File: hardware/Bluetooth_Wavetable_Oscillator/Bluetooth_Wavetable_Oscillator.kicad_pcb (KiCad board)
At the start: 2 copper layers, 48 x 110 mm, 65 parts, among them J1 2x5 Connector, J2 AudioJack2, J3 AudioJack2_SwitchT, J4 AudioJack2_SwitchT, SW1 SW_Push, U1 L7805, U2 ESP32-WROOM-32D, U3 MCP4821, U4 TL074, U5 TL072, U6 NE5532

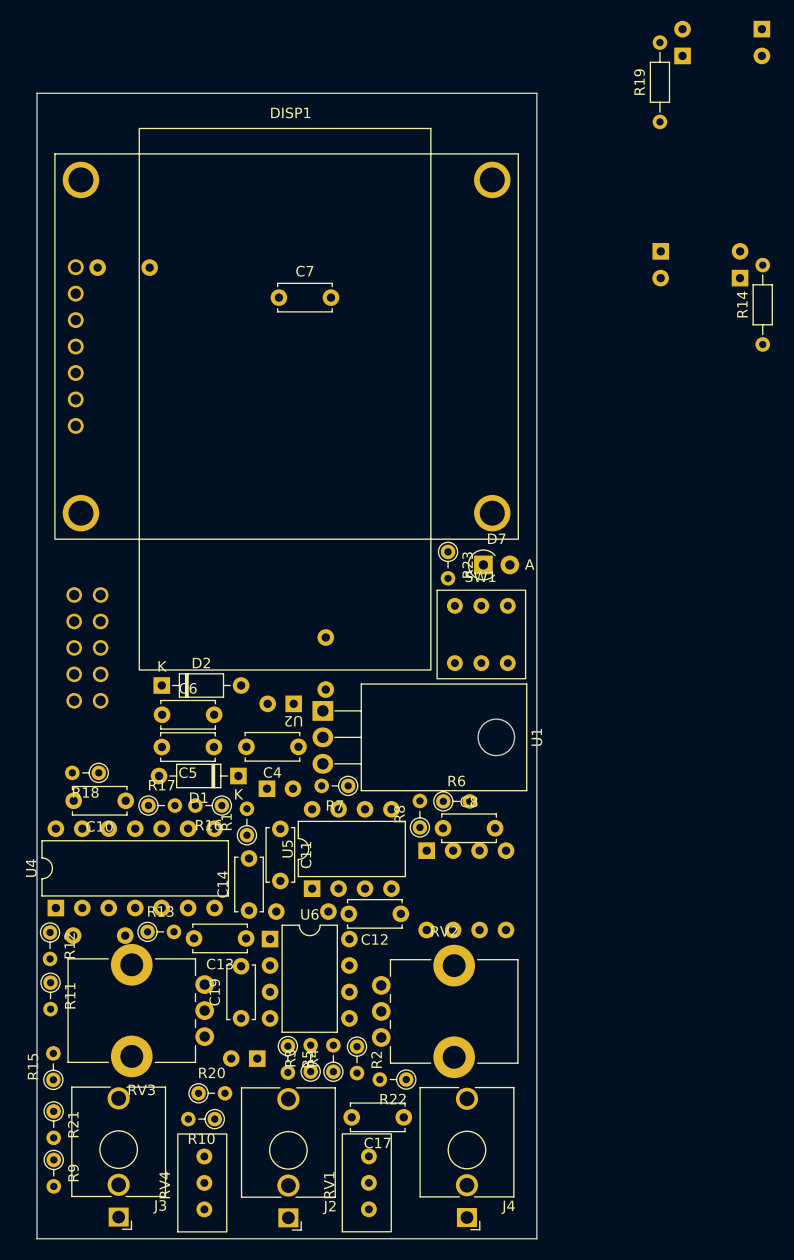
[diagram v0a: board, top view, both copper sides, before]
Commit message: update shematic, PCB and footprints
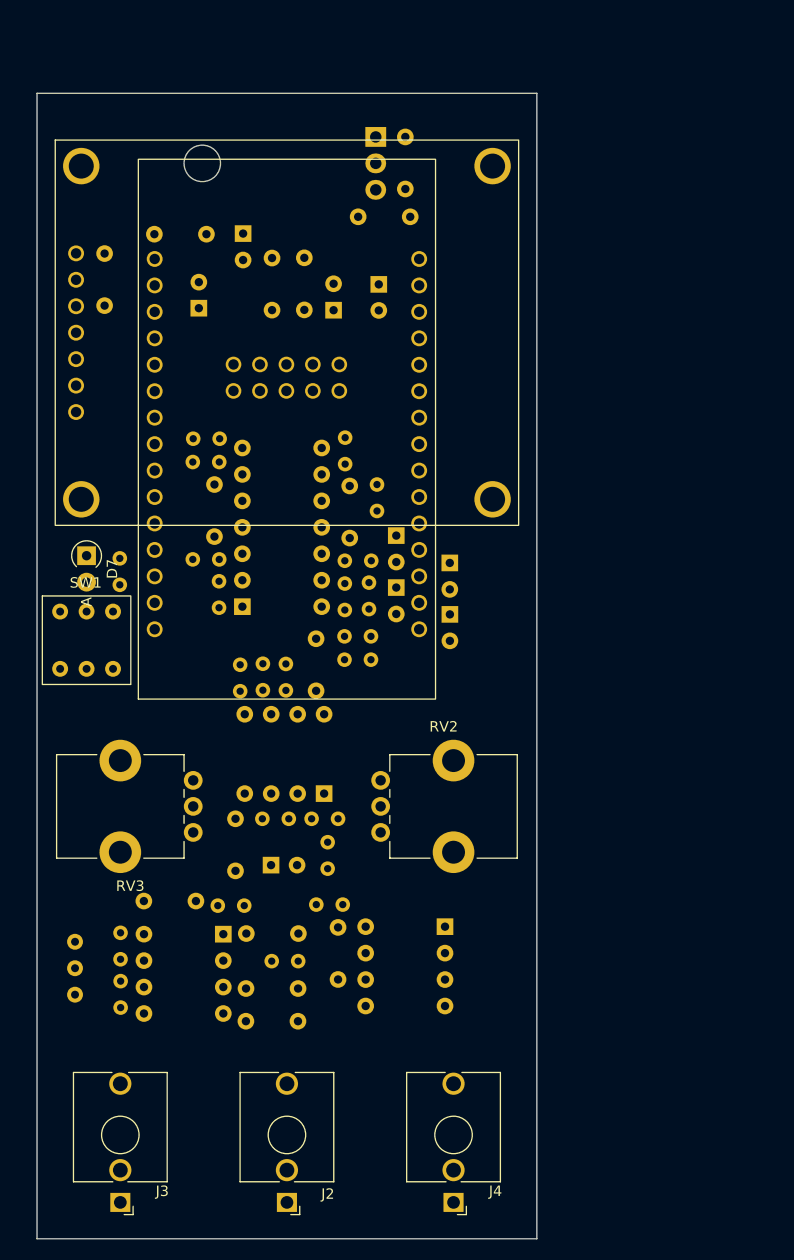
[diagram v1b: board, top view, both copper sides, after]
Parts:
- removed C17: 0.1u, Capacitor_THT:C_Disc_D5.0mm_W2.5mm_P5.00mm
- removed RV1: 10k, Trimmer-potentiometer:Trimmer-potentiometer
- C10, C11, C12, C13, C14, C19, C4, C5, C6, C7, C8, R1, R10, R11, R12, R13, R15, R16, R17, R18, R2, R20, R21, R22, R23, R3, R5, R6, R7, R8, R9, RV4, U1, U4, U5, U6: moved to B.Cu
- D1, D2: footprint Diode_THT:D_DO-35_SOD27_P7.62mm_Horizontal -> Diode_THT:D_DO-35_SOD27_P2.54mm_Vertical_KathodeUp; moved to B.Cu
- D3, D4, D5, D6: footprint Diode_THT:D_DO-35_SOD27_P7.62mm_Horizontal -> Diode_THT:D_DO-35_SOD27_P2.54mm_Vertical_KathodeUp
- R14, R19: footprint Resistor_THT:R_Axial_DIN0204_L3.6mm_D1.6mm_P7.62mm_Horizontal -> Resistor_THT:R_Axial_DIN0204_L3.6mm_D1.6mm_P2.54mm_Vertical; moved to B.Cu
- R4: value 10k -> 1k; moved to B.Cu
- moved R15 62.9 mm to (153.7, 85.4)
- moved D6 60.0 mm to (155.6, 87.8), turned to -90 degrees
- moved D5 58.0 mm to (155.6, 92.8), turned to -90 degrees
- moved R19 57.9 mm to (150.6, 97.4), turned to 0 degrees
- moved U1 55.4 mm to (153.6, 49.5)
- moved R10 53.8 mm to (136.0, 90.0), turned to 0 degrees
- moved C1 53.6 mm to (156.4, 49.5), turned to -90 degrees
- moved D1 52.1 mm to (140.8, 58.8), turned to -90 degrees
- moved C4 51.2 mm to (151.9, 57.1), turned to 0 degrees
- moved R9 50.8 mm to (140.6, 100.2)
- moved R14 50.3 mm to (150.6, 99.7), turned to 0 degrees
- moved R12 48.0 mm to (138.6, 80.7), turned to 180 degrees
- moved R13 47.9 mm to (138.6, 78.5), turned to 180 degrees
- moved C5 47.3 mm to (143.6, 61.1), turned to -90 degrees
- moved C2 46.6 mm to (136.6, 65.9), turned to 90 degrees
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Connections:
- R4 pad 1: /Output/-1.024V -> Net-(R4-Pad1)
- R4 pad 2: Net-(U6B--) -> Net-(J2-PadT)
- R5 pad 2: Net-(J2-PadT) -> Net-(R4-Pad1)
- U6 pad 7: Net-(J2-PadT) -> Net-(R4-Pad1)

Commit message: all items connected
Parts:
- D3, D4, D5, D6: footprint Diode_THT:D_DO-35_SOD27_P2.54mm_Vertical_KathodeUp -> Diode_THT:D_DO-34_SOD68_P7.62mm_Horizontal
- R1, R2, R20, R3, R4, R5, R6, R7: footprint Resistor_THT:R_Axial_DIN0204_L3.6mm_D1.6mm_P2.54mm_Vertical -> Resistor_THT:R_Axial_DIN0204_L3.6mm_D1.6mm_P7.62mm_Horizontal
- moved R7 12.6 mm to (138.3, 104.4), turned to 0 degrees
- moved R6 12.2 mm to (138.4, 106.7), turned to -90 degrees
- moved D4 11.5 mm to (160.5, 101.8), turned to 90 degrees
- moved R8 11.1 mm to (133.9, 103.7)
- moved R5 10.3 mm to (138.8, 136.6), turned to 180 degrees
- moved R20 9.57 mm to (156.3, 123.3), turned to 180 degrees
- moved U5 9.44 mm to (141.1, 106.8), turned to -90 degrees
- moved R9 9.42 mm to (131.7, 103.3)
- moved D6 7.37 mm to (155.0, 80.4)
- moved R21 7.31 mm to (136.2, 105.8)
- moved C7 7.13 mm to (132.1, 54.0), turned to -90 degrees
- moved R3 5.47 mm to (146.4, 123.3)
- moved C16 4.93 mm to (148.4, 119.1)
- moved R15 4.69 mm to (152.8, 80.8)
- moved R10 4.66 mm to (136.3, 94.7), turned to 90 degrees
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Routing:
- net +3.3V: track 0.00 -> 183.2 mm
- net -12V: track 0.00 -> 177.7 mm
- net /DAC_CS: track 0.00 -> 150.3 mm, vias 0 -> 1
- net +12V: track 0.00 -> 146.3 mm
- net /DAC_MOSI: track 0.00 -> 73.5 mm
- net Net-(J3-PadTN): track 0.00 -> 66.0 mm
- net /DAC_SCK: track 0.00 -> 65.1 mm
- net +5V: track 0.00 -> 64.0 mm
- net Net-(J4-PadT): track 0.00 -> 58.9 mm
- net Net-(J4-PadTN): track 0.00 -> 55.8 mm
- net Net-(R10-Pad1): track 0.00 -> 39.4 mm
- net /DISP_MOSI: track 0.00 -> 36.5 mm
- net Net-(R13-Pad2): track 0.00 -> 35.0 mm
- net /BTH_SWITCH: track 0.00 -> 28.9 mm
- net /DISP_SCK: track 0.00 -> 21.6 mm
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- added copper zone on In1.Cu, net GND
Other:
- copper layers 2 -> 4

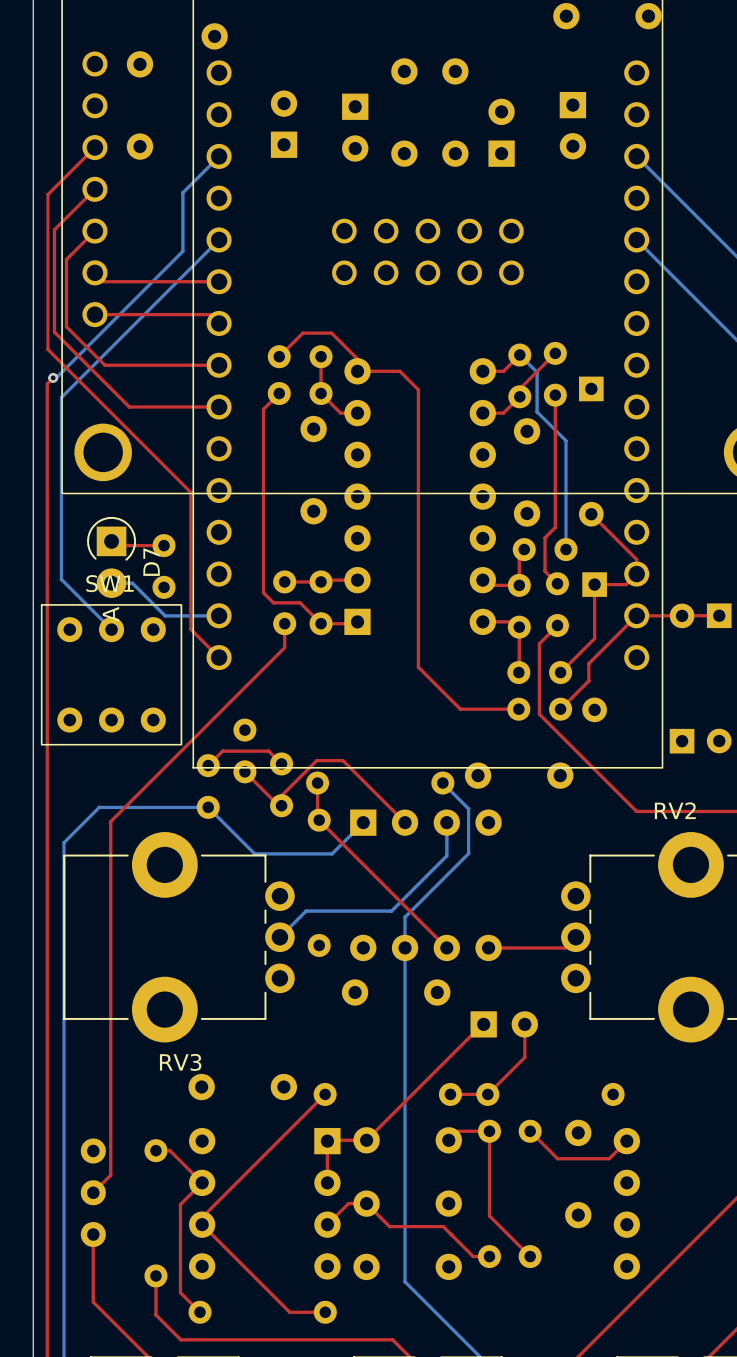
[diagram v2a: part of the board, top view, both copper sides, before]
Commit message: fix silkscreen clipping
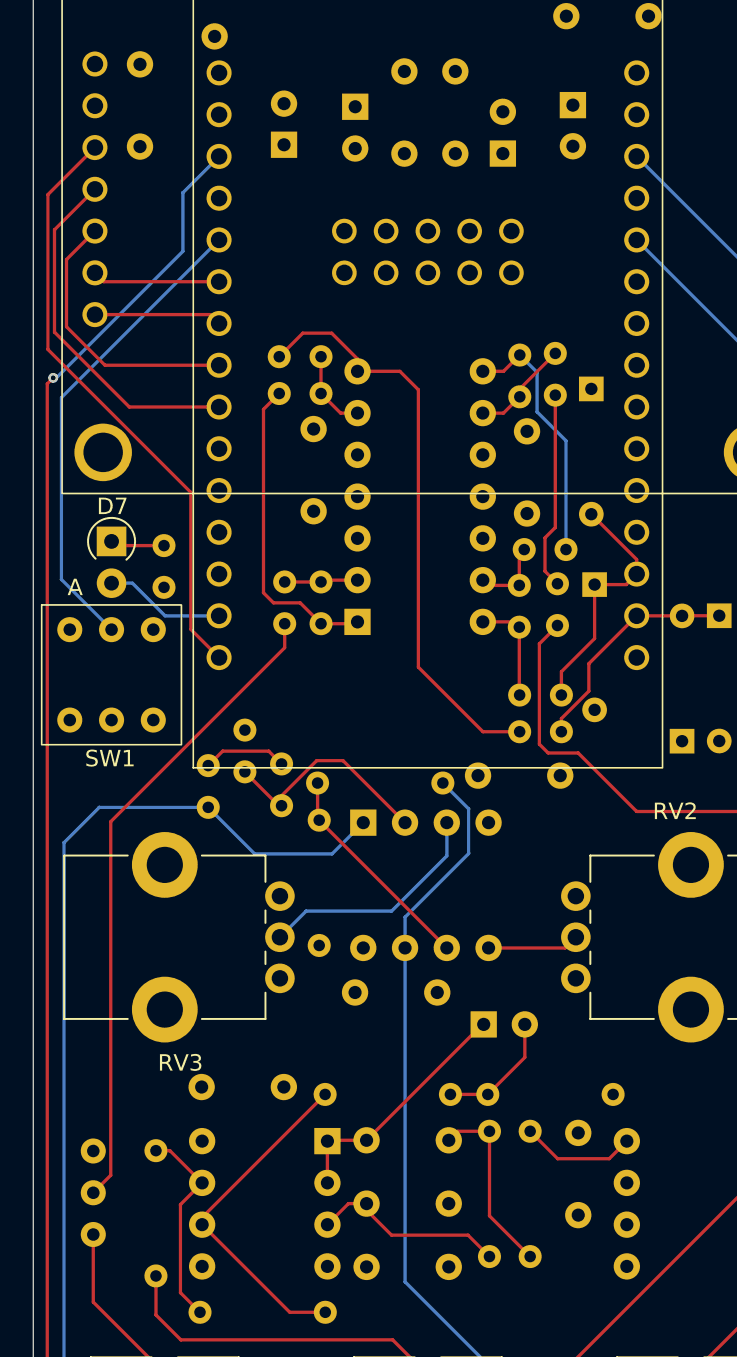
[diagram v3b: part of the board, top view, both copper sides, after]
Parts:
- moved R19 1.37 mm to (150.6, 99.0)
- moved R14 1.37 mm to (150.6, 101.3)
- moved D2 0.08 mm to (149.6, 66.1)
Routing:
- net Net-(R18-Pad2): track 5.12 -> 6.49 mm
- net POSITION: track 13.8 -> 15.2 mm
- net PITCH: track 12.6 -> 14.0 mm
- net Net-(J4-PadT): track 58.9 -> 59.9 mm
- net Net-(R13-Pad2): track 35.0 -> 35.6 mm
